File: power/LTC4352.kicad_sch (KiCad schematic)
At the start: 15 parts, among them Q1 Si7336ADP, U1 LTC4352CMS

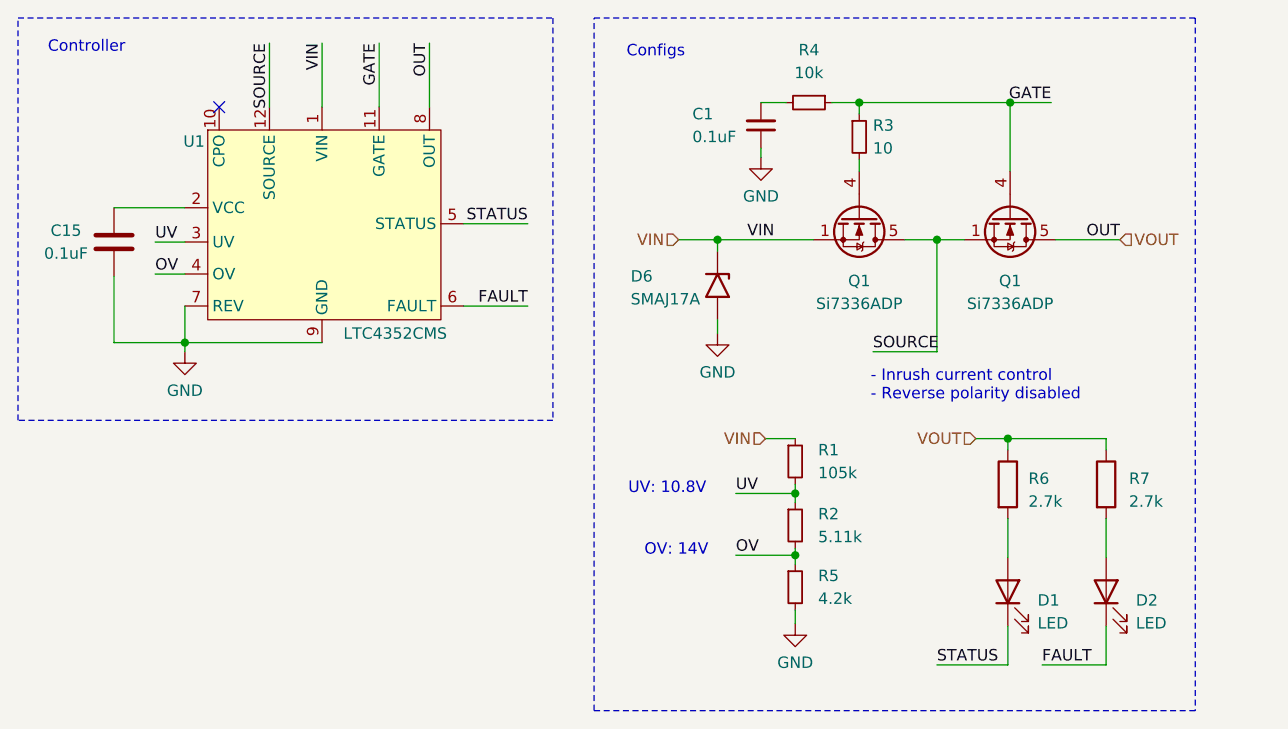
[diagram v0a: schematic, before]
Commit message: Feat[power]: footprints assigned, initial layout
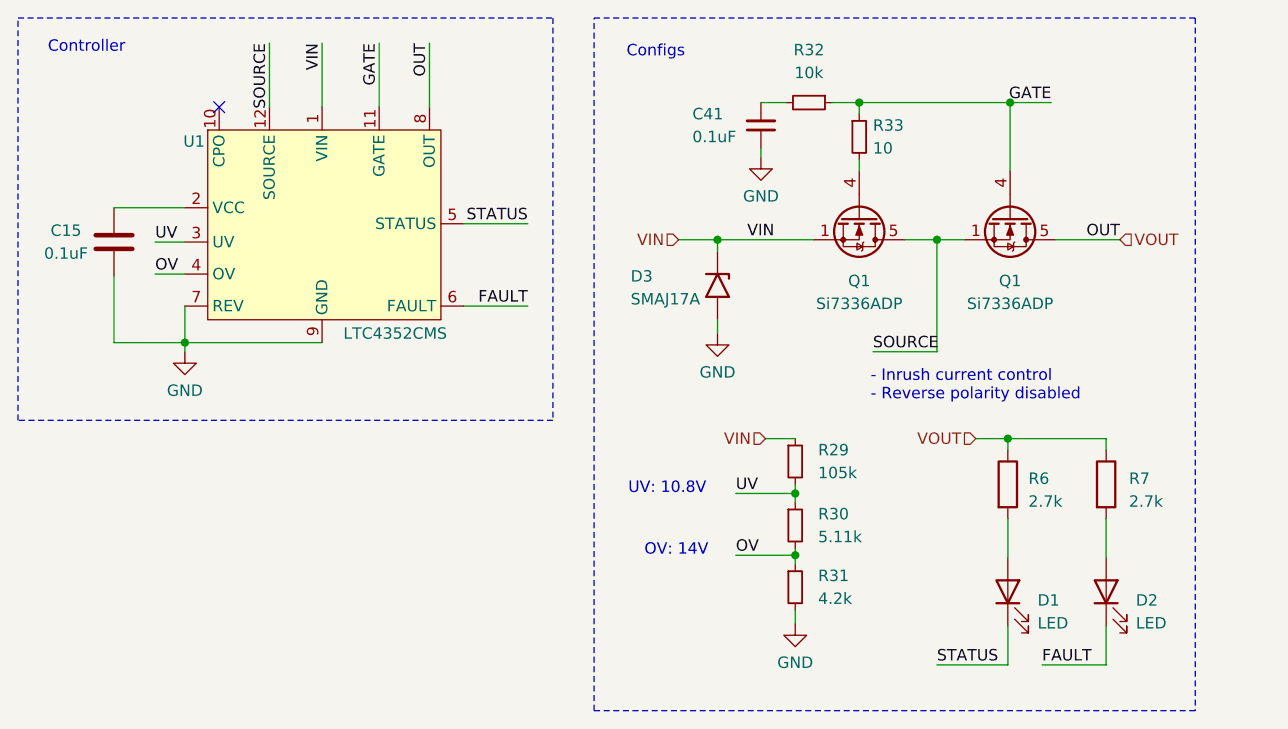
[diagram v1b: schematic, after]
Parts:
- C41: renamed from C1; footprint (none) -> Capacitor_SMD:C_0603_1608Metric
- D1: footprint Power:LED_15-21SYGC_S530-E2_TR8 -> LED_SMD:LED_0603_1608Metric
- D2: footprint Power:RESC1005X38N -> LED_SMD:LED_0603_1608Metric
- R29: renamed from R1; footprint (none) -> Resistor_SMD:R_0603_1608Metric
- R30: renamed from R2; footprint (none) -> Resistor_SMD:R_0603_1608Metric
- R31: renamed from R5; footprint (none) -> Resistor_SMD:R_0603_1608Metric
- R32: renamed from R4; footprint (none) -> Resistor_SMD:R_0603_1608Metric
- R33: renamed from R3; footprint (none) -> Resistor_SMD:R_0603_1608Metric
- renumbered D6 to D3
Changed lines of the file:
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@@
         )
         (path "/6d3c5c52-febb-4c99-82d7-f9b22bb5762b/d3c479b7-f7bf-4296-8fee-4e35418d9676"
-          (reference "#PWR01") (unit 1)
+          (reference "#PWR021") (unit 1)
         )
       )
@@
   (symbol (lib_id "Diode:SMAJ17A") (at 156.21 95.504 270) (unit 1)
     (exclude_from_sim no) (in_bom yes) (on_board yes) (dnp no)
-    (property "Reference" "D6" (at 146.558 94.488 90)
+    (property "Reference" "D3" (at 146.558 94.488 90)
       (effects (font (size 1.27 1.27)) (justify left))
     )
@@
       (project "power"
         (path "/6d3c5c52-febb-4c99-82d7-f9b22bb5762b/d3c479b7-f7bf-4296-8fee-4e35418d9676"
-          (reference "D6") (unit 1)
+          (reference "D3") (unit 1)
         )
       )
@@
         )
         (path "/6d3c5c52-febb-4c99-82d7-f9b22bb5762b/d3c479b7-f7bf-4296-8fee-4e35418d9676"
-          (reference "R7") (unit 1)
+          (reference "R35") (unit 1)
         )
       )
@@
       (effects (font (size 1.27 1.27)) (justify right))
     )
-    (property "Footprint" "Power:RESC1005X38N" (at 199.39 129.54 0)
+    (property "Footprint" "LED_SMD:LED_0603_1608Metric" (at 199.39 129.54 0)
       (effects (font (size 1.27 1.27)) hide)
     )
@@
         )
         (path "/6d3c5c52-febb-4c99-82d7-f9b22bb5762b/d3c479b7-f7bf-4296-8fee-4e35418d9676"
-          (reference "D2") (unit 1)
+          (reference "D5") (unit 1)
         )
       )
@@
   (symbol (lib_id "Device:C_Small") (at 161.036 77.724 180) (unit 1)
     (exclude_from_sim no) (in_bom yes) (on_board yes) (dnp no)
-    (property "Reference" "C1" (at 153.416 76.454 0)
+    (property "Reference" "C41" (at 153.416 76.454 0)
       (effects (font (size 1.27 1.27)) (justify right))
     )
@@
       (effects (font (size 1.27 1.27)) (justify right))
     )
-    (property "Footprint" "" (at 161.036 77.724 0)
+    (property "Footprint" "Capacitor_SMD:C_0603_1608Metric" (at 161.036 77.724 0)
       (effects (font (size 1.27 1.27)) hide)
     )
@@
       (project "power"
         (path "/6d3c5c52-febb-4c99-82d7-f9b22bb5762b/d3c479b7-f7bf-4296-8fee-4e35418d9676"
-          (reference "C1") (unit 1)
+          (reference "C41") (unit 1)
         )
       )
@@
   (symbol (lib_id "Device:R_Small") (at 166.37 75.184 270) (unit 1)
     (exclude_from_sim no) (in_bom yes) (on_board yes) (dnp no) (fields_autoplaced)
-    (property "Reference" "R4" (at 166.37 69.342 90)
+    (property "Reference" "R32" (at 166.37 69.342 90)
       (effects (font (size 1.27 1.27)))
     )
@@
       (effects (font (size 1.27 1.27)))
     )
-    (property "Footprint" "" (at 166.37 75.184 0)
+    (property "Footprint" "Resistor_SMD:R_0603_1608Metric" (at 166.37 75.184 0)
       (effects (font (size 1.27 1.27)) hide)
     )
@@
       (project "power"
         (path "/6d3c5c52-febb-4c99-82d7-f9b22bb5762b/d3c479b7-f7bf-4296-8fee-4e35418d9676"
-          (reference "R4") (unit 1)
+          (reference "R32") (unit 1)
         )
       )
@@
         )
         (path "/6d3c5c52-febb-4c99-82d7-f9b22bb5762b/d3c479b7-f7bf-4296-8fee-4e35418d9676"
-          (reference "#PWR03") (unit 1)
+          (reference "#PWR023") (unit 1)
         )
       )
@@
         )
         (path "/6d3c5c52-febb-4c99-82d7-f9b22bb5762b/d3c479b7-f7bf-4296-8fee-4e35418d9676"
-          (reference "#PWR013") (unit 1)
+          (reference "#PWR020") (unit 1)
         )
       )
@@
       (effects (font (size 1.27 1.27)) (justify right))
     )
-    (property "Footprint" "Power:LED_15-21SYGC_S530-E2_TR8" (at 188.468 129.54 0)
+    (property "Footprint" "LED_SMD:LED_0603_1608Metric" (at 188.468 129.54 0)
       (effects (font (size 1.27 1.27)) hide)
     )
@@
         )
         (path "/6d3c5c52-febb-4c99-82d7-f9b22bb5762b/d3c479b7-f7bf-4296-8fee-4e35418d9676"
-          (reference "D1") (unit 1)
+          (reference "D4") (unit 1)
         )
       )
@@
         )
         (path "/6d3c5c52-febb-4c99-82d7-f9b22bb5762b/d3c479b7-f7bf-4296-8fee-4e35418d9676"
-          (reference "#PWR02") (unit 1)
+          (reference "#PWR022") (unit 1)
         )
       )
@@
         )
         (path "/6d3c5c52-febb-4c99-82d7-f9b22bb5762b/d3c479b7-f7bf-4296-8fee-4e35418d9676"
-          (reference "R6") (unit 1)
+          (reference "R34") (unit 1)
         )
       )
@@
         )
         (path "/6d3c5c52-febb-4c99-82d7-f9b22bb5762b/d3c479b7-f7bf-4296-8fee-4e35418d9676"
-          (reference "C15") (unit 1)
+          (reference "C40") (unit 1)
         )
       )
@@
   (symbol (lib_id "Device:R_Small") (at 164.846 129.032 0) (unit 1)
     (exclude_from_sim no) (in_bom yes) (on_board yes) (dnp no) (fields_autoplaced)
-    (property "Reference" "R5" (at 167.386 127.762 0)
+    (property "Reference" "R31" (at 167.386 127.762 0)
       (effects (font (size 1.27 1.27)) (justify left))
     )
@@
       (effects (font (size 1.27 1.27)) (justify left))
     )
-    (property "Footprint" "" (at 164.846 129.032 0)
+    (property "Footprint" "Resistor_SMD:R_0603_1608Metric" (at 164.846 129.032 0)
       (effects (font (size 1.27 1.27)) hide)
     )
@@
       (project "power"
         (path "/6d3c5c52-febb-4c99-82d7-f9b22bb5762b/d3c479b7-f7bf-4296-8fee-4e35418d9676"
-          (reference "R5") (unit 1)
+          (reference "R31") (unit 1)
         )
       )
@@
   (symbol (lib_id "Device:R_Small") (at 164.846 122.174 0) (unit 1)
     (exclude_from_sim no) (in_bom yes) (on_board yes) (dnp no) (fields_autoplaced)
-    (property "Reference" "R2" (at 167.386 120.904 0)
+    (property "Reference" "R30" (at 167.386 120.904 0)
       (effects (font (size 1.27 1.27)) (justify left))
     )
@@
       (effects (font (size 1.27 1.27)) (justify left))
     )
-    (property "Footprint" "" (at 164.846 122.174 0)
+    (property "Footprint" "Resistor_SMD:R_0603_1608Metric" (at 164.846 122.174 0)
       (effects (font (size 1.27 1.27)) hide)
     )
@@
       (project "power"
         (path "/6d3c5c52-febb-4c99-82d7-f9b22bb5762b/d3c479b7-f7bf-4296-8fee-4e35418d9676"
-          (reference "R2") (unit 1)
+          (reference "R30") (unit 1)
         )
       )
@@
   (symbol (lib_id "Device:R_Small") (at 171.958 78.994 0) (unit 1)
     (exclude_from_sim no) (in_bom yes) (on_board yes) (dnp no) (fields_autoplaced)
-    (property "Reference" "R3" (at 173.482 77.724 0)
+    (property "Reference" "R33" (at 173.482 77.724 0)
       (effects (font (size 1.27 1.27)) (justify left))
     )
@@
       (effects (font (size 1.27 1.27)) (justify left))
     )
-    (property "Footprint" "" (at 171.958 78.994 0)
+    (property "Footprint" "Resistor_SMD:R_0603_1608Metric" (at 171.958 78.994 0)
       (effects (font (size 1.27 1.27)) hide)
     )
@@
       (project "power"
         (path "/6d3c5c52-febb-4c99-82d7-f9b22bb5762b/d3c479b7-f7bf-4296-8fee-4e35418d9676"
-          (reference "R3") (unit 1)
+          (reference "R33") (unit 1)
         )
       )
@@
   (symbol (lib_id "Device:R_Small") (at 164.846 115.062 0) (unit 1)
     (exclude_from_sim no) (in_bom yes) (on_board yes) (dnp no) (fields_autoplaced)
-    (property "Reference" "R1" (at 167.386 113.792 0)
+    (property "Reference" "R29" (at 167.386 113.792 0)
       (effects (font (size 1.27 1.27)) (justify left))
     )
@@
       (effects (font (size 1.27 1.27)) (justify left))
     )
-    (property "Footprint" "" (at 164.846 115.062 0)
+    (property "Footprint" "Resistor_SMD:R_0603_1608Metric" (at 164.846 115.062 0)
       (effects (font (size 1.27 1.27)) hide)
     )
@@
       (project "power"
         (path "/6d3c5c52-febb-4c99-82d7-f9b22bb5762b/d3c479b7-f7bf-4296-8fee-4e35418d9676"
-          (reference "R1") (unit 1)
+          (reference "R29") (unit 1)
         )
       )
@@
         )
         (path "/6d3c5c52-febb-4c99-82d7-f9b22bb5762b/d3c479b7-f7bf-4296-8fee-4e35418d9676"
-          (reference "U1") (unit 1)
-        )
-      )
+          (reference "U4") (unit 1)
+        )
+      )

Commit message: Feat[power]: v2.1 schematic complete
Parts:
- removed R31: 4.2k, Resistor_SMD:R_0603_1608Metric, symbol Device:R_Small
- added R20: 100k, Resistor_SMD:R_0603_1608Metric, symbol Device:R_Small
- added R21: 3k, Resistor_SMD:R_0603_1608Metric, symbol Device:R_Small
- D3: value SMAJ17A -> SMAJ14A
- Q1: value Si7336ADP -> SIRA00DP
- renumbered C41 to C29, R29 to R17, R30 to R18, R32 to R19, R33 to R22
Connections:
- net GND: now also R18.2, R21.2
- net OV: now also R20.2, R21.1; no longer R18.2
- net SOURCE: now also Q1.1 (S), Q1.2 (S), Q1.3 (S); no longer Q1.5 (D)
- net VIN: now also Q1.5 (D), R20.1; no longer Q1.1 (S), Q1.2 (S), Q1.3 (S)
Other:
- note added: "Inrush current control"
- note added: "OV: 17V"
- note added: "R_{ds} = 1mOhm at 10V I_{peak} = 25A 25^{2}*1 = 0.625W"
- note added: "Reverse polarity disabled"
- note added: "Vz_{min} = 15.6V"
- note removed: "- Inrush current control - Reverse polarity disabled"
- note removed: "OV: 14V"
- moved on the sheet: Q1, R17, R18, R22

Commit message: Feat[power]: component mapping
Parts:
- R17: value 105k -> 100k
- R18: value 5.11k -> 5.1k
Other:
- note added: "UV: 10.3V"
- note removed: "UV: 10.8V"
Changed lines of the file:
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@@
     (effects (font (size 1.27 1.27)) (justify left))
   )
-  (text "UV: 10.8V" (exclude_from_sim no)
+  (text "UV: 10.3V" (exclude_from_sim no)
  (at 147.32 121.158 0)
     (effects (font (size 1.27 1.27)))
@@
   (symbol (lib_id "Device:R_Small") (at 153.924 121.92 0) (unit 1)
     (exclude_from_sim no) (in_bom yes) (on_board yes) (dnp no) (fields_autoplaced)
-    (property "Reference" "R18" (at 156.464 120.65 0)
-      (effects (font (size 1.27 1.27)) (justify left))
-    )
-    (property "Value" "5.11k" (at 156.464 123.19 0)
+    (property "Reference" "R18" (at 156.21 120.65 0)
+      (effects (font (size 1.27 1.27)) (justify left))
+    )
+    (property "Value" "5.1k" (at 156.21 123.19 0)
       (effects (font (size 1.27 1.27)) (justify left))
     )
@@
   (symbol (lib_id "Device:R_Small") (at 153.924 114.808 0) (unit 1)
     (exclude_from_sim no) (in_bom yes) (on_board yes) (dnp no) (fields_autoplaced)
-    (property "Reference" "R17" (at 156.464 113.538 0)
-      (effects (font (size 1.27 1.27)) (justify left))
-    )
-    (property "Value" "105k" (at 156.464 116.078 0)
-      (effects (font (size 1.27 1.27)) (justify left))
-    )
+    (property "Reference" "R17" (at 156.21 113.538 0)
+      (effects (font (size 1.27 1.27)) (justify left))
+    )
+    (property "Value" "100k" (at 156.21 116.078 0)
+      (effects (font (size 1.27 1.27)) (justify left))
+    )

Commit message: Feat: float sid
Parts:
- added D7: D, symbol Device:D
- renumbered C15 to C28, D1 to D4, D2 to D5, Q1 to Q2, R6 to R23, R7 to R24, U1 to U3
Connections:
- net VOUT: now also D7.1 (K)
